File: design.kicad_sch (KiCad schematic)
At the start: 33 parts, among them J1 490107670412, J2 TYPE-C-31-M-12, J4 Conn_02x02_Counter_Clockwise, U1 AP2112K-3.3, U2 TCK107AF,LF, U3 CH340C, U4 TS3USB30RSWR

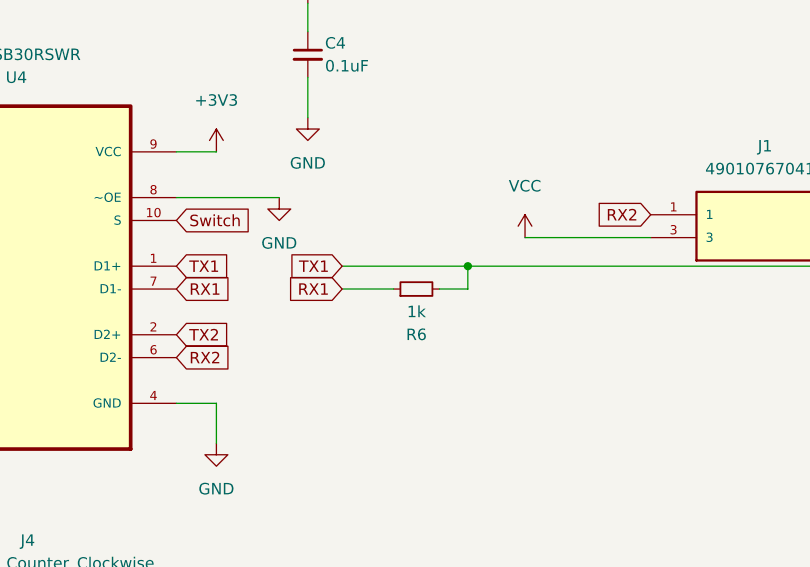
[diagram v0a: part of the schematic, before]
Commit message: correct serialUPDI resistor
the correct way is in the TX line
add picture of serialUPDI wiring
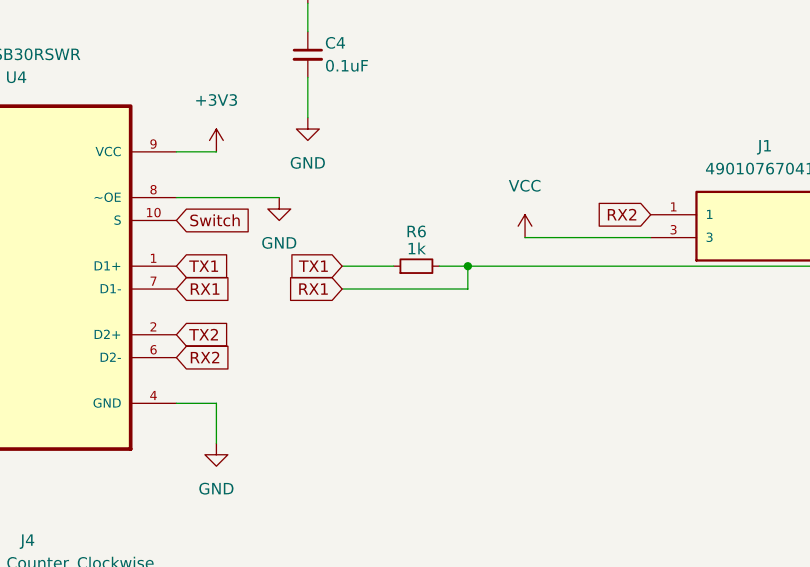
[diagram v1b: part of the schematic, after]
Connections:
- net RX1: now also J1.4, R6.2; no longer R6.1
- net TX1: now also R6.1; no longer J1.4, R6.2
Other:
- moved on the sheet: R6

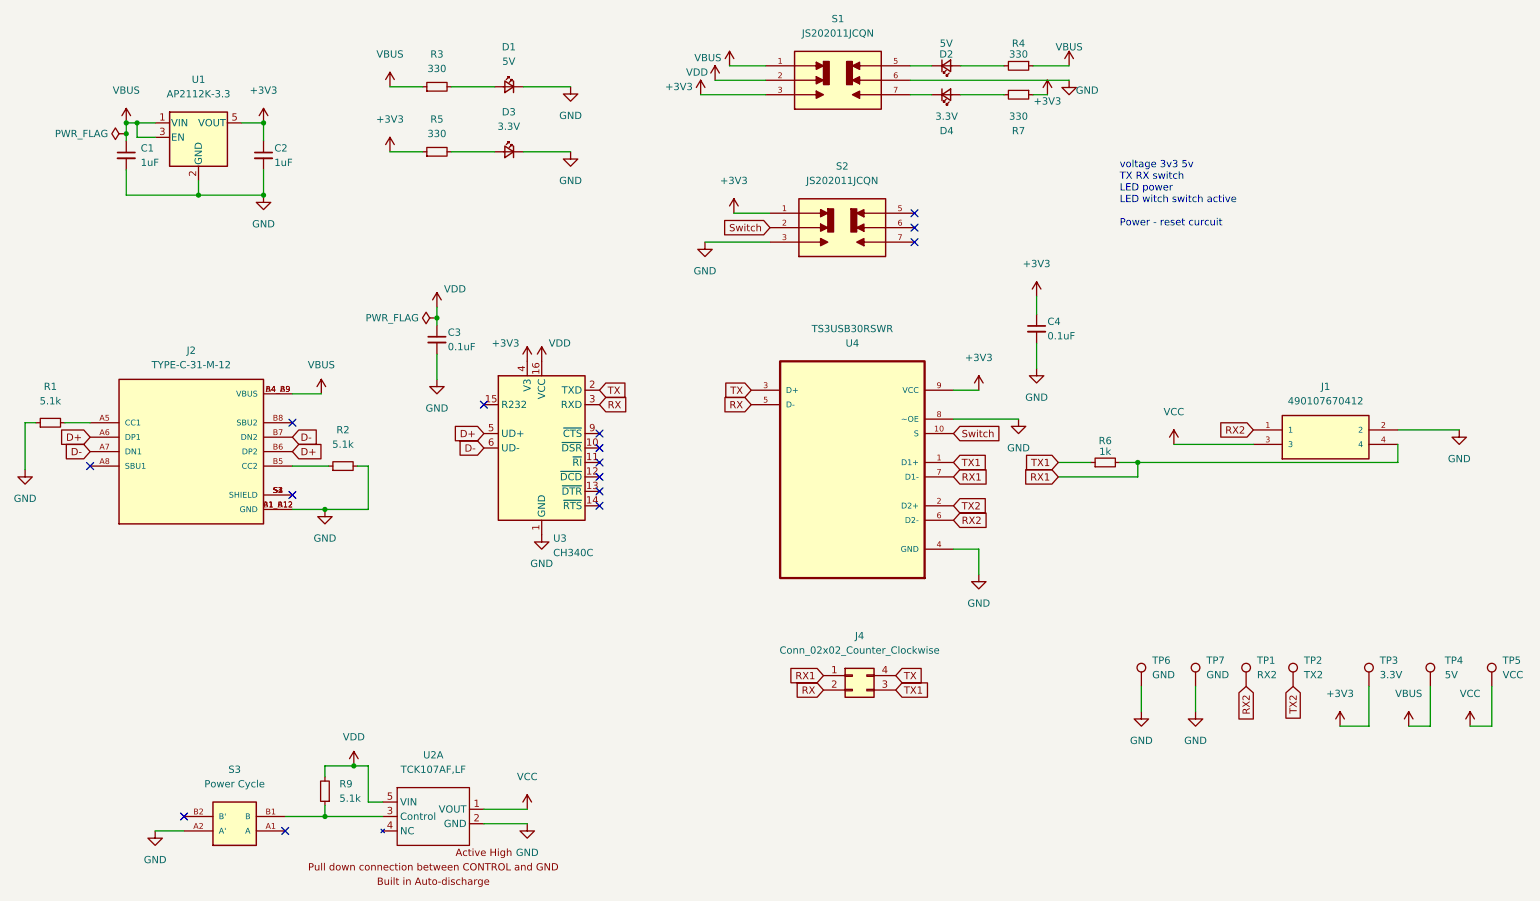
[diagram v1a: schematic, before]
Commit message: Add DTR automatic switching and Testpoints
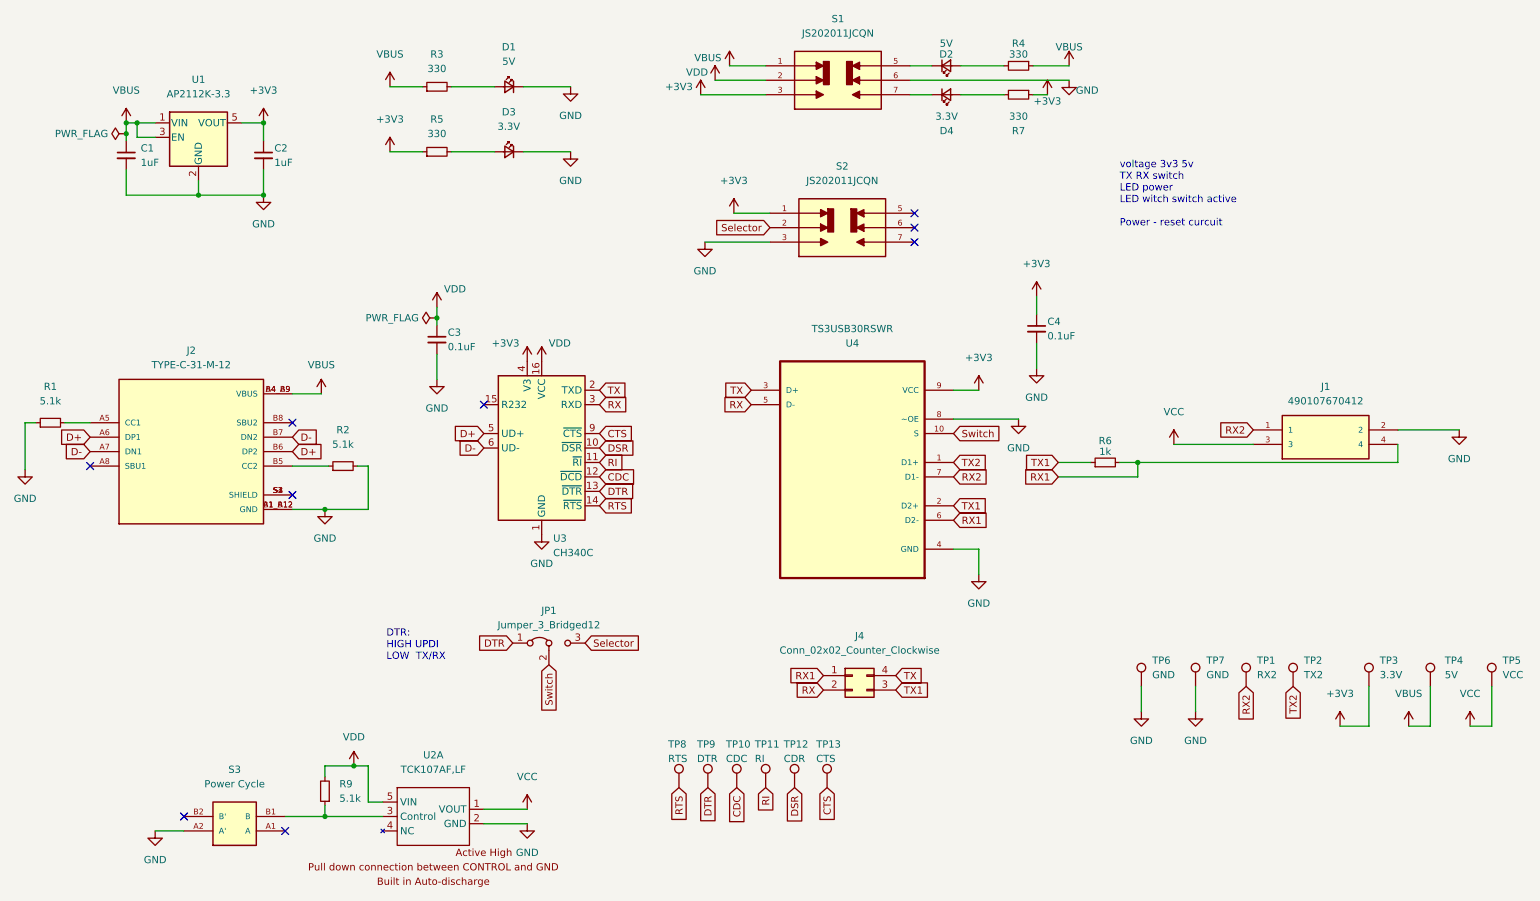
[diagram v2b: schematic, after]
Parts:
- added JP1: Jumper_3_Bridged12, Jumper:SolderJumper-3_P1.3mm_Bridged12_Pad1.0x1.5mm_NumberLabels, symbol Jumper:Jumper_3_Bridged12
- added TP10: CDC, TestPoint:TestPoint_Pad_D1.0mm, symbol Connector:TestPoint
- added TP11: RI, TestPoint:TestPoint_Pad_D1.0mm, symbol Connector:TestPoint
- added TP12: CDR, TestPoint:TestPoint_Pad_D1.0mm, symbol Connector:TestPoint
- added TP13: CTS, TestPoint:TestPoint_Pad_D1.0mm, symbol Connector:TestPoint
- added TP8: RTS, TestPoint:TestPoint_Pad_D1.0mm, symbol Connector:TestPoint
- added TP9: DTR, TestPoint:TestPoint_Pad_D1.0mm, symbol Connector:TestPoint
- TP6, TP7: footprint TestPoint:TestPoint_Pad_D2.0mm -> TestPoint:TestPoint_Pad_D1.0mm
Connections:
- net RX1: now also U4.6 (D2-); no longer U4.7 (D1-)
- net RX2: now also U4.7 (D1-); no longer U4.6 (D2-)
- net Switch: now also JP1.2 (C); no longer S2.2
- net TX1: now also U4.2 (D2+); no longer U4.1 (D1+)
- net TX2: now also U4.1 (D1+); no longer U4.2 (D2+)
- net DSR: now reaches U3.10 (~{DSR})
- net DSR: now also TP12.1
- net RI: now reaches U3.11 (~{RI})
- net RI: now also TP11.1
- net CDC: now reaches U3.12 (~{DCD})
- net CDC: now also TP10.1
- net DTR: now reaches U3.13 (~{DTR})
- net DTR: now also JP1.1 (A), TP9.1
- net RTS: now reaches U3.14 (~{RTS})
- net RTS: now also TP8.1
- net CTS: now reaches U3.9 (~{CTS})
- net CTS: now also TP13.1
- new net Selector: JP1.3 (B), S2.2
- no-connect marks 15 -> 9
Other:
- note added: "DTR: HIGH UPDI LOW TX/RX"
